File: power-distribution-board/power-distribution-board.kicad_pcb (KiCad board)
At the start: 2 copper layers, 90 x 70 mm, 24 parts, among them J1 Conn_01x02, J2 Conn_01x02, J3 Conn_01x02, J4 Conn_01x02, J5 Conn_01x02, J6 Conn_01x02, J7 Conn_01x02, J8 Conn_01x02

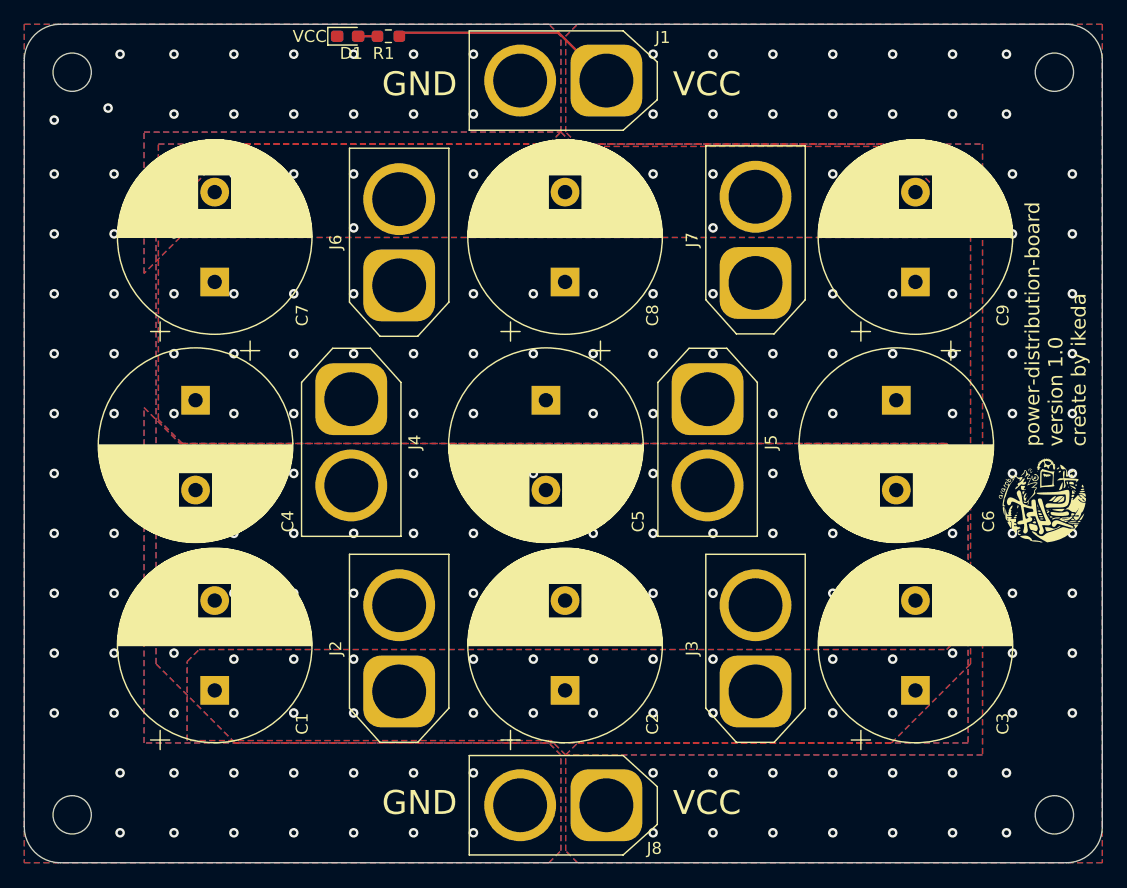
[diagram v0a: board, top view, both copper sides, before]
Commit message: ±の反転を修正 ガーバ生成
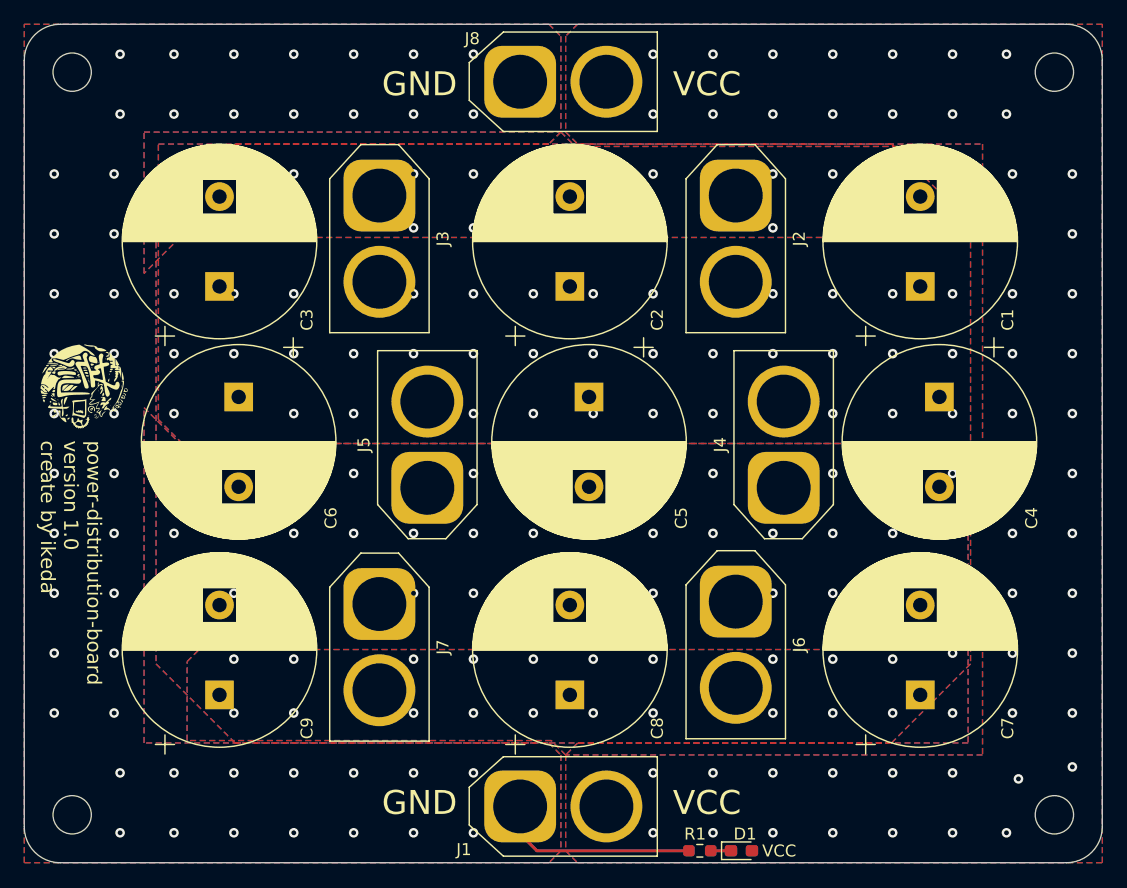
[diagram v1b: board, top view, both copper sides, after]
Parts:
- moved REF** 102.8 mm to (19.0, 19.0), turned to 180 degrees
- moved REF** 102.8 mm to (101.0, 19.0), turned to 180 degrees
- moved REF** 102.8 mm to (19.0, 81.0), turned to 180 degrees
- moved REF** 102.8 mm to (101.0, 81.0), turned to 180 degrees
- moved G*** 81.3 mm to (19.7, 45.0), turned to -90 degrees
- moved D1 75.5 mm to (74.9, 84.0)
- moved R1 72.8 mm to (71.4, 84.0)
- moved C7 68.2 mm to (89.8, 71.0)
- moved C1 67.9 mm to (89.8, 36.9)
- moved C9 67.6 mm to (31.3, 71.0)
- moved C3 67.2 mm to (31.3, 36.9)
- moved C4 62.1 mm to (91.4, 46.1)
- moved J1 61.0 mm to (56.4, 80.3), turned to 0 degrees
- moved J8 60.8 mm to (56.4, 19.8), turned to 0 degrees
- moved C6 54.9 mm to (32.9, 46.1)
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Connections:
- D1 pad 1: GND -> Net-(D1-K)
- D1 pad 2: Net-(D1-A) -> VCC
- J1 pad 1: VCC -> GND
- J1 pad 2: GND -> VCC
- J2 pad 1: VCC -> GND
- J2 pad 2: GND -> VCC
- J3 pad 1: VCC -> GND
- J3 pad 2: GND -> VCC
- J4 pad 1: VCC -> GND
- J4 pad 2: GND -> VCC
- J5 pad 1: VCC -> GND
- J5 pad 2: GND -> VCC
- J6 pad 1: VCC -> GND
- J6 pad 2: GND -> VCC
- J7 pad 1: VCC -> GND
- J7 pad 2: GND -> VCC
- J8 pad 1: VCC -> GND
- J8 pad 2: GND -> VCC
- R1 pad 1: VCC -> Net-(D1-K)
- R1 pad 2: Net-(D1-A) -> GND
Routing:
- net VCC: track 19.1 -> 0.00 mm, vias 106 -> 110
- net GND: track 0.00 -> 17.0 mm, vias 110 -> 106
- net Net-(D1-K): track 0.00 -> 1.69 mm
- net Net-(D1-A): track 1.57 -> 0.00 mm
